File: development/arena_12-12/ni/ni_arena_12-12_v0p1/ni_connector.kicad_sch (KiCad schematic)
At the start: 29 parts, among them J2 NI_TE_68pos

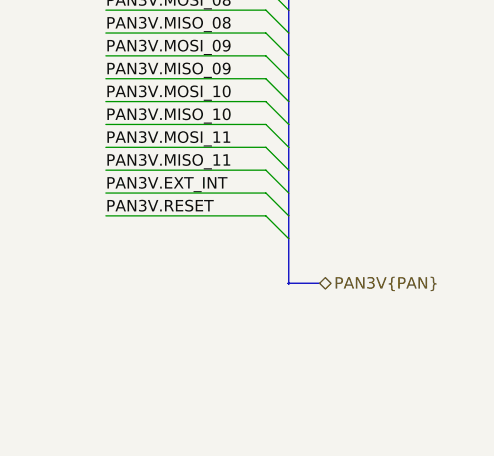
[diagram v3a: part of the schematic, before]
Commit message: Worked on NI 12-12 arena schematic.
Set up new bus definitions and started working through DRC issues.
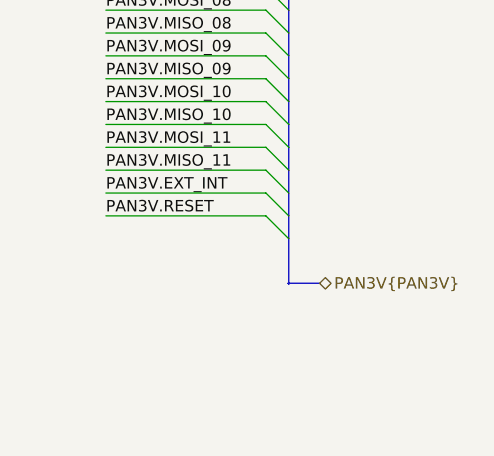
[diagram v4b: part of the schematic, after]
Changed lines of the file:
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@@
 	(generator_version "8.0")
 	(paper "A4")
+	(bus_alias "PAN3V"
+		(members "CS_0" "CS_1" "CS_2" "CS_3" "CS_4" "CS_5" "CS_6" "CS_7" "SCK_0"
+			"SCK_1" "SCK_2" "SCK_3" "SCK_4" "SCK_5" "MOSI_00" "MISO_00" "MOSI_01"
+			"MISO_01" "MOSI_02" "MISO_02" "MOSI_03" "MISO_04" "MOSI_05" "MISO_05"
+			"MOSI_06" "MISO_06" "MOSI_07" "MISO_07" "MOSI_08" "MISO_08" "MOSI_09"
+			"MISO_09" "MOSI_10" "MISO_10" "MOSI_11" "MISO_11" "EXT_INT" "RESET"
+		)
+	)
 	(junction
 		(at 86.487 125.857)
@@
 		)
 	)
-	(hierarchical_label "PAN3V{PAN}"
+	(hierarchical_label "PAN3V{PAN3V}"
 		(shape bidirectional)
 		(at 196.469 131.953 0)

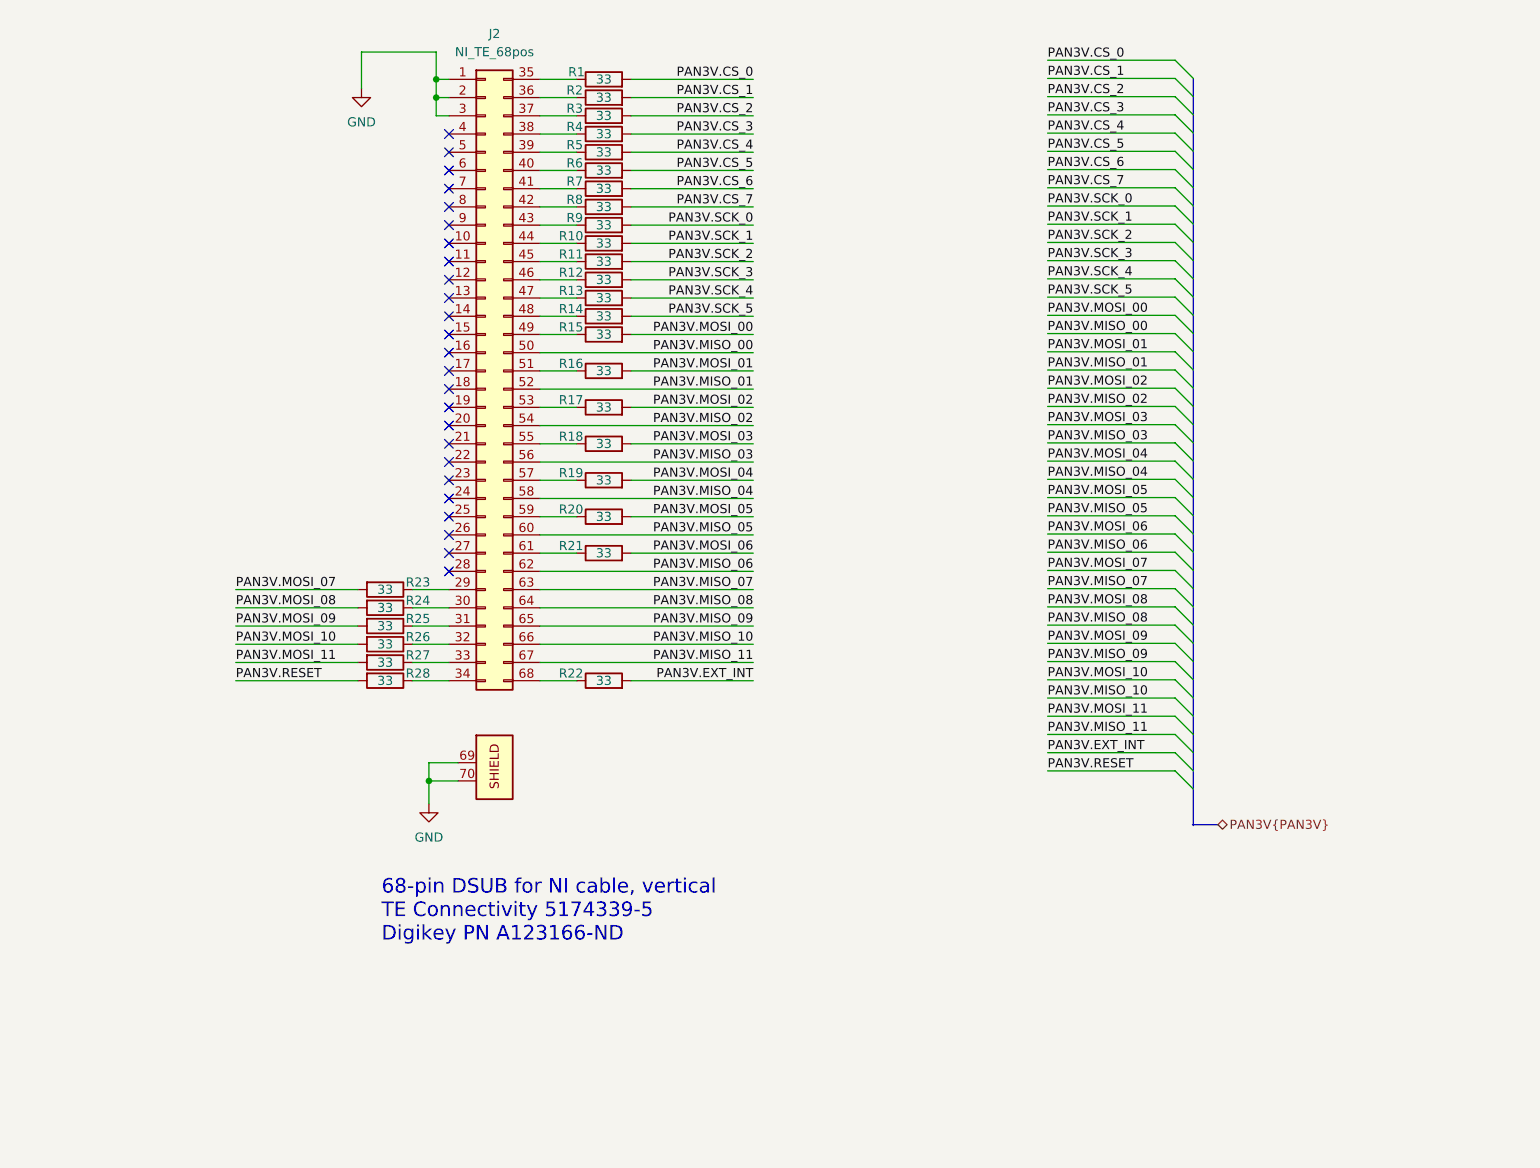
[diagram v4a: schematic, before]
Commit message: ERC for NI 12-12 arena with schmitt buffers now passing.
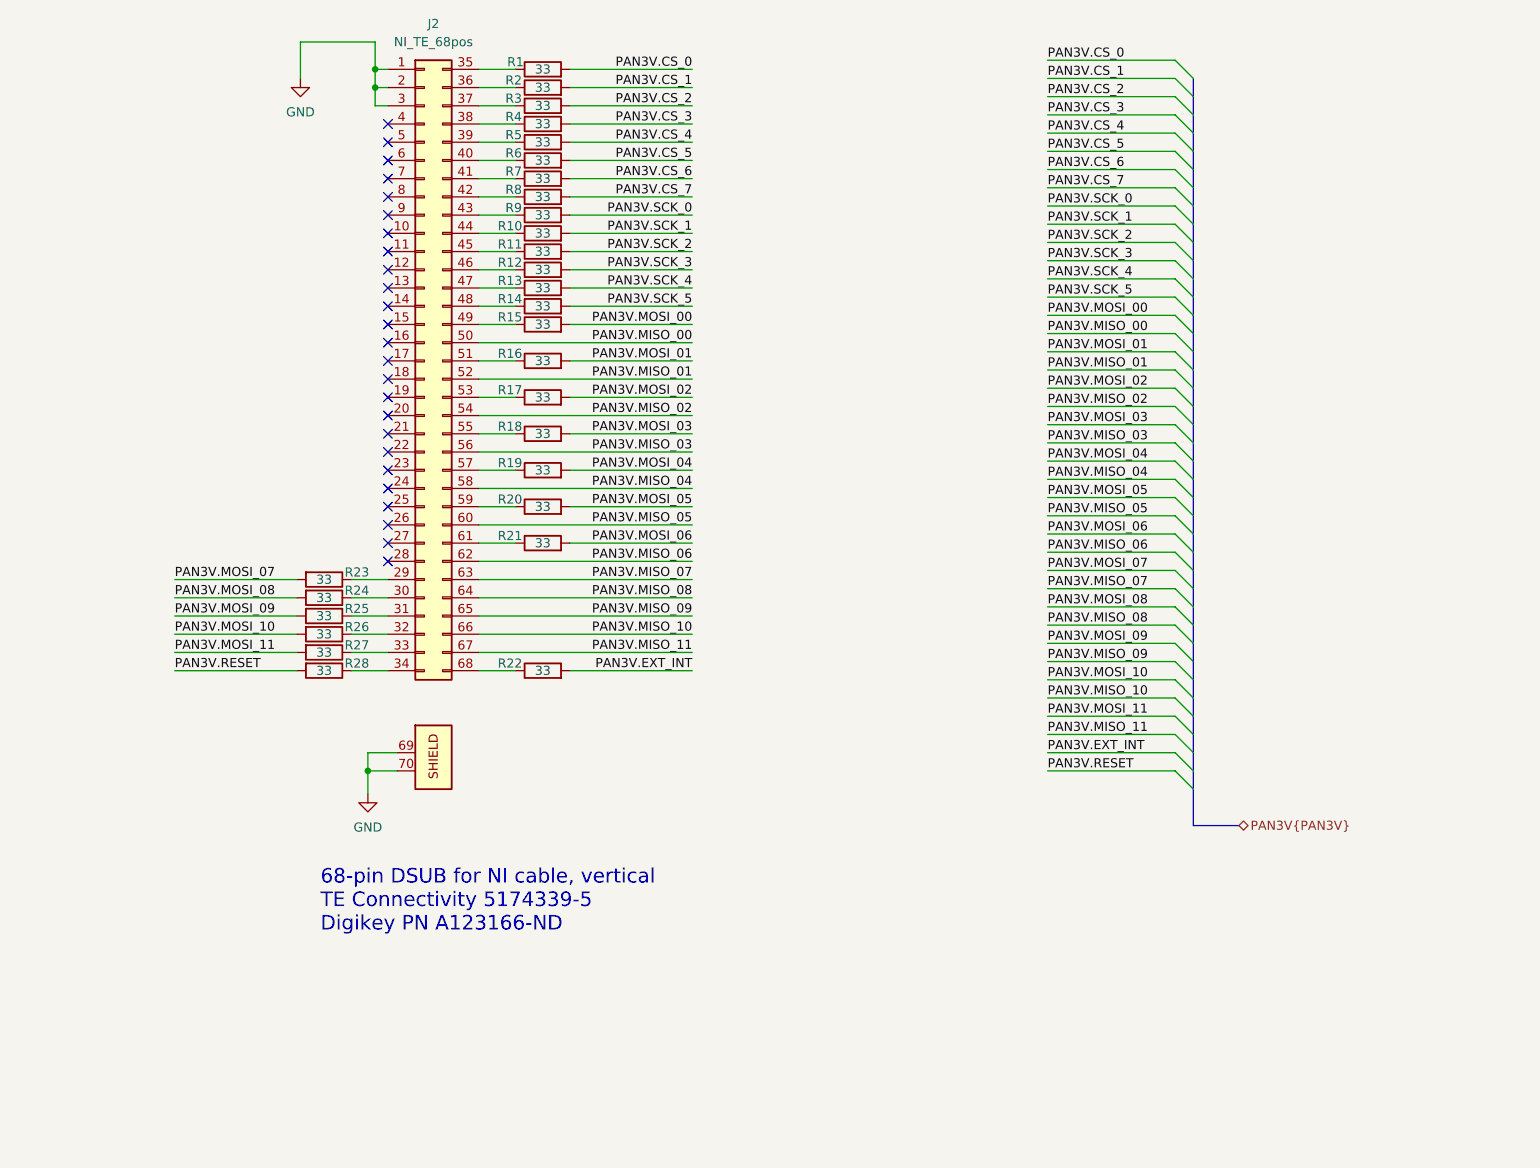
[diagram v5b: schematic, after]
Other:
- moved on the sheet: J2, R1, R10, R11, R12, R13, R14, R15, R16, R17, R18, R19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

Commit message: Worked on 12-12 NI arena with schmitt buffers.
Finished footprint assignments.
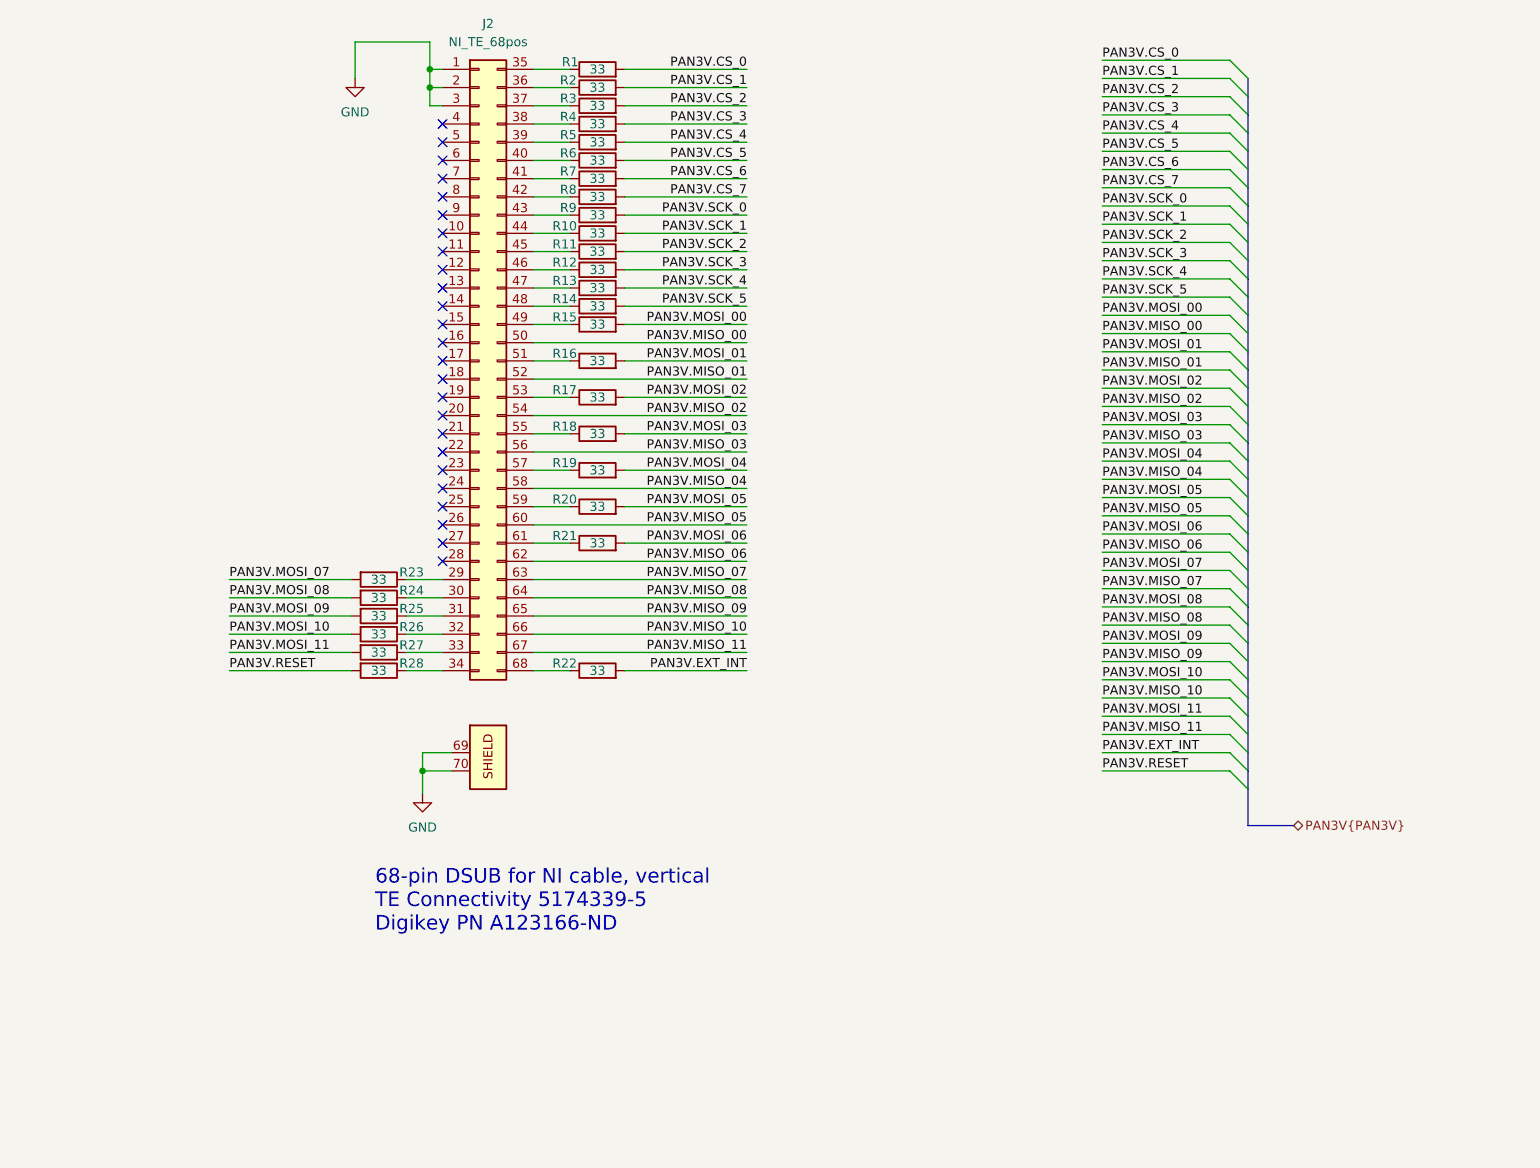
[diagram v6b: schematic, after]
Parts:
- J2: footprint (none) -> Capacitor_SMD:C_1206_3216Metric
- R1, R10, R11, R12, R13, R14, R15, R16, R17, R18, R19, R2, R20, R21, R22, R23, R24, R25, R26, R27, R28, R3, R4, R5, R6, R7, R8, R9: footprint (none) -> Resistor_SMD:R_0402_1005Metric
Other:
- moved on the sheet: J2, R1, R10, R11, R12, R13, R14, R15, R16, R17, R18, R19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

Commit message: Wored on layout for 12-12 NI arena with schmitt buffers.
Worked on layout for schmitt buffers and series term. resitors around
at the base of a panel column.
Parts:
- J2: footprint Capacitor_SMD:C_1206_3216Metric -> arena_custom:TE_CONN_DSUB_VERT_68
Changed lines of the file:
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@@
 			)
 		)
-		(property "Footprint" "Capacitor_SMD:C_1206_3216Metric"
+		(property "Footprint" "arena_custom:TE_CONN_DSUB_VERT_68"
 			(at 93.472 67.31 0)
 			(effects
